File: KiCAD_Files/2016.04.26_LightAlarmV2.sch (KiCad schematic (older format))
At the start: 18 parts, among them P1 CONN_01X03, P2 CONN_01X05, P3 USB_B, SW1 SW_PUSH, SW2 SW_PUSH, U1 LM1117-SOT-223, U2 ESP-12E

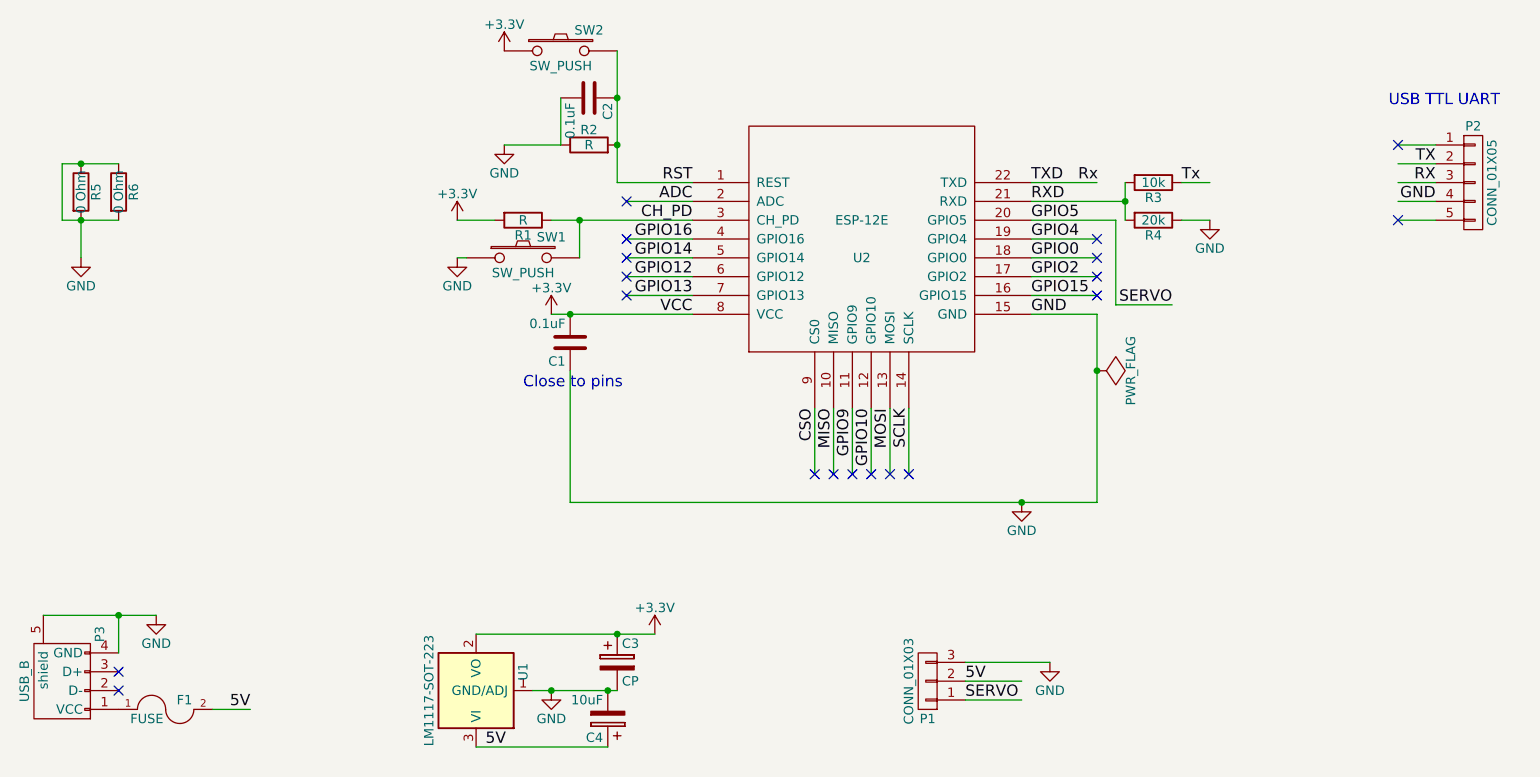
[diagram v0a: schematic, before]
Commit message: Added button to allow for reflashing firmware
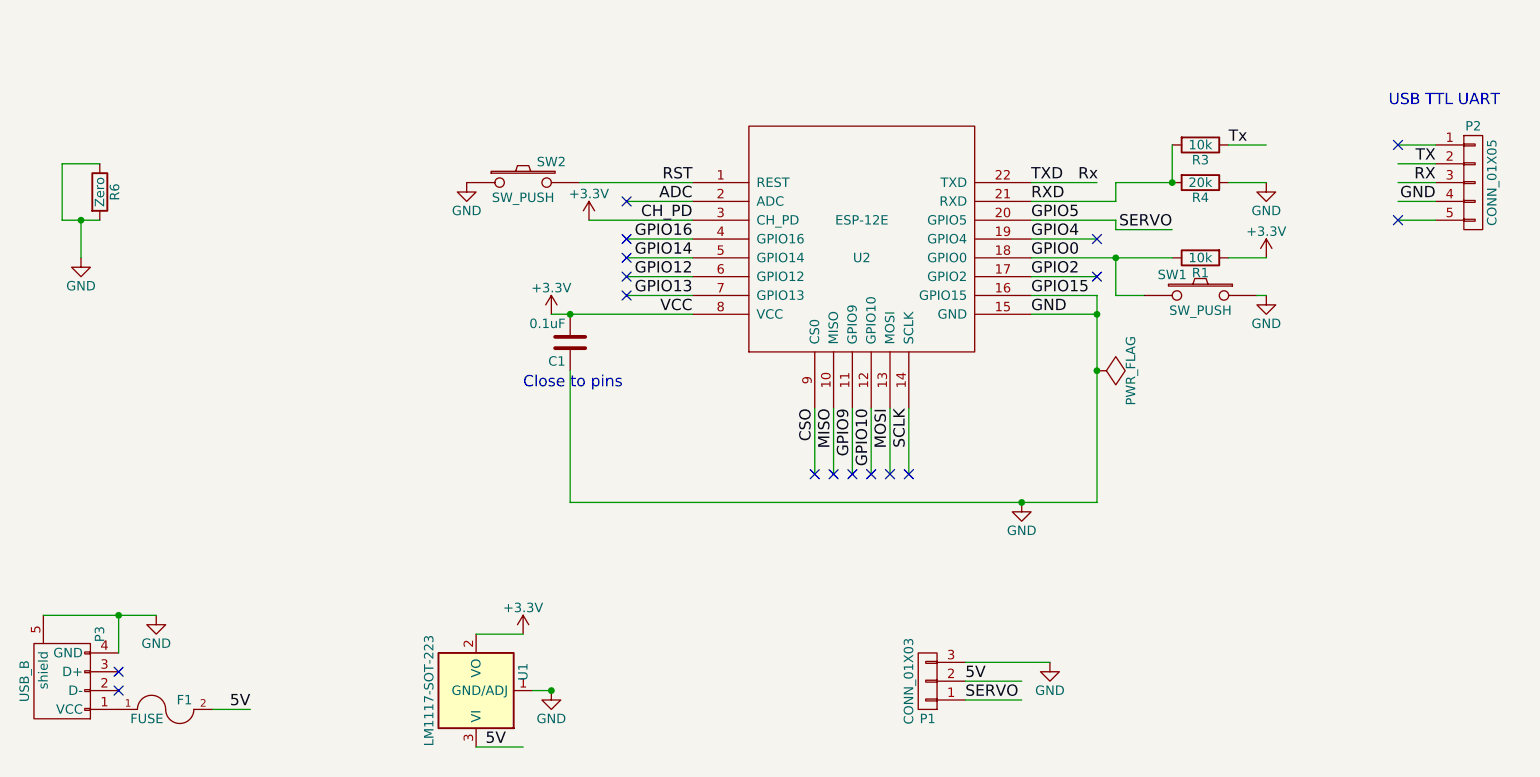
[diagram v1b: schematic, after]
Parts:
- removed C2: 0.1uF, Resistors_SMD:R_0805_HandSoldering, symbol C
- removed C3: CP, Capacitors_Tantalum_SMD:TantalC_SizeS_EIA-3216, symbol CP
- removed C4: 10uF, Capacitors_Tantalum_SMD:TantalC_SizeS_EIA-3216, symbol CP
- removed R2: R, Resistors_SMD:R_0805_HandSoldering, symbol R
- removed R5: 0 Ohm, Resistors_SMD:R_1206_HandSoldering, symbol R
- R1: value R -> 10k
- R6: value 0 Ohm -> Zero
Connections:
- no-connect marks 19 -> 17
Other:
- moved on the sheet: R1, R3, R4, R6, SW1, SW2
